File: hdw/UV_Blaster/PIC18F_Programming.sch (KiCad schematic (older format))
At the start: 10 parts

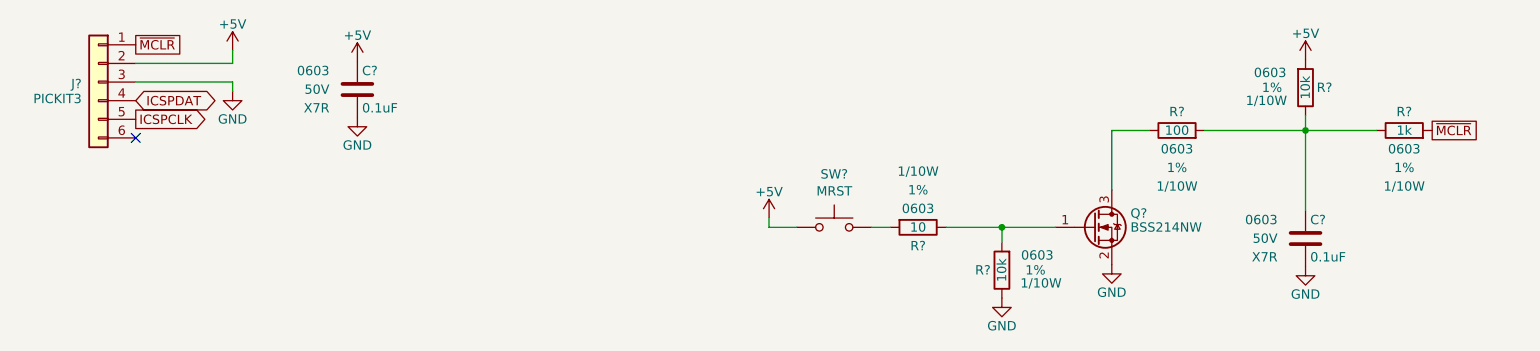
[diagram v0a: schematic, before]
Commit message: More sch work, netlist, part numbers, footprints
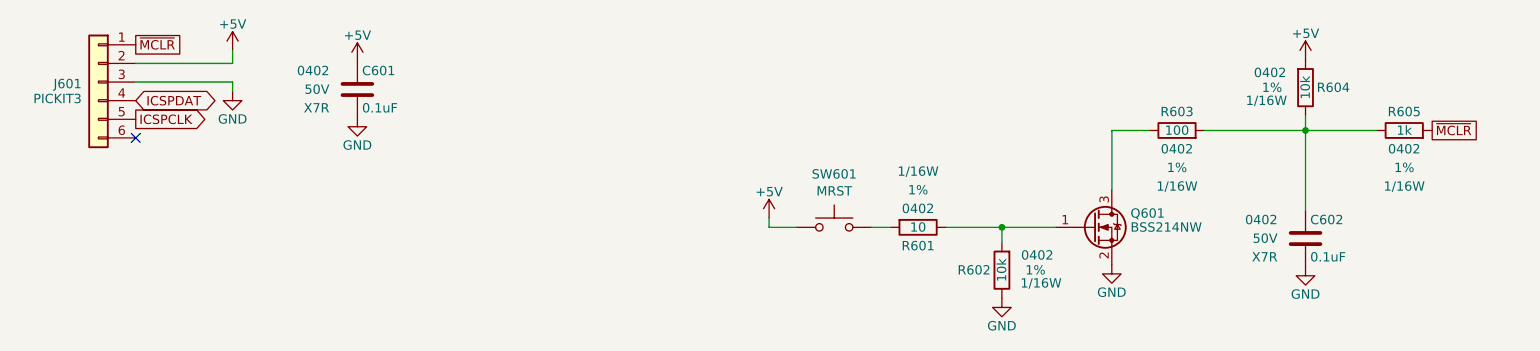
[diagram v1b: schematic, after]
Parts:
- C601, C602: renamed from C?; footprint Capacitors_SMD:C_0603 -> Capacitors_SMD:C_0402; Digi-Key PN 311-1344-1-ND -> 490-10701-1-ND; display_footprint 0603 -> 0402
- R601: renamed from R?; footprint Resistors_SMD:R_0603 -> Resistors_SMD:R_0402; Digi-Key PN YAG3351CT-ND -> 311-10.0LRCT-ND; Wattage 1/10W -> 1/16W; display_footprint 0603 -> 0402
- R602, R604: renamed from R?; footprint Resistors_SMD:R_0603 -> Resistors_SMD:R_0402; Digi-Key PN RMCF0603FT10K0CT-ND -> 541-3959-1-ND; Wattage 1/10W -> 1/16W; display_footprint 0603 -> 0402
- R603: renamed from R?; footprint Resistors_SMD:R_0603 -> Resistors_SMD:R_0402; Digi-Key PN A106047CT-ND -> 311-100LRCT-ND; Wattage 1/10W -> 1/16W; display_footprint 0603 -> 0402
- R605: renamed from R?; footprint Resistors_SMD:R_0603 -> Resistors_SMD:R_0402; Digi-Key PN RMCF0603FT1K00CT-ND -> P1.00KLCT-ND; Wattage 1/10W -> 1/16W; display_footprint 0603 -> 0402
- gave numbers to parts that had none: 3
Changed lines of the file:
@@
 encoding utf-8
 Sheet 6 14
-Title "QI Charger"
-Date "2019-01-03"
+Title "UV Blaster"
+Date "2020-05-07"
 Rev "A"
-Comp ""
+Comp "Drew Maatman"
 Comment1 ""
 Comment2 ""
@@
 $EndDescr
 $Comp
-L Connector_Generic:Conn_01x06 J?
+L Connector_Generic:Conn_01x06 J601
 U 1 1 5BB4A695
 P 1070 1990
-F 0 "J?" H 1160 1980 50  0000 L CNN
+F 0 "J601" H 1160 1980 50  0000 L CNN
 F 1 "PICKIT3" H 1160 1900 50  0000 L CNN
 F 2 "Custom Footprints Library:PICKIT3_Header" H 1070 1990 50  0001 C CNN
@@
 ICSPCLK
 $Comp
-L power:GND #PWR?
+L power:GND #PWR0602
 U 1 1 5BB4A7C4
 P 1790 2040
-F 0 "#PWR?" H 1790 1790 50  0001 C CNN
+F 0 "#PWR0602" H 1790 1790 50  0001 C CNN
 F 1 "GND" H 1790 1890 50  0000 C CNN
 F 2 "" H 1790 2040 50  0001 C CNN
@@
 NoConn ~ 1270 2290
 $Comp
-L Custom_Library:C_Custom C?
+L Custom_Library:C_Custom C601
 U 1 1 5BC13497
 P 2460 2030
-F 0 "C?" H 2485 2130 50  0000 L CNN
+F 0 "C601" H 2485 2130 50  0000 L CNN
 F 1 "0.1uF" H 2485 1930 50  0000 L CNN
-F 2 "Capacitors_SMD:C_0603" H 2498 1880 50  0001 C CNN
+F 2 "Capacitors_SMD:C_0402" H 2498 1880 50  0001 C CNN
 F 3 "" H 2485 2130 50  0001 C CNN
-F 4 "0603" H 2310 2130 50  0000 R CNN "display_footprint"
+F 4 "0402" H 2310 2130 50  0000 R CNN "display_footprint"
 F 5 "50V" H 2310 2030 50  0000 R CNN "Voltage"
 F 6 "X7R" H 2310 1930 50  0000 R CNN "Dielectric"
-F 7 "311-1344-1-ND" H 2885 2530 60  0001 C CNN "Digi-Key PN"
+F 7 "490-10701-1-ND" H 2885 2530 60  0001 C CNN "Digi-Key PN"
 	1    2460 2030
 	1    0    0    -1
 $EndComp
 $Comp
-L power:GND #PWR?
+L power:GND #PWR0604
 U 1 1 5BC1349E
 P 2460 2180
-F 0 "#PWR?" H 2460 1930 50  0001 C CNN
+F 0 "#PWR0604" H 2460 1930 50  0001 C CNN
 F 1 "GND" H 2460 2030 50  0000 C CNN
 F 2 "" H 2460 2180 50  0001 C CNN
@@
 AR Path="/5BAAE16C/5BC152E5" Ref="R?"  Part="1"
 AR Path="/5C1D5CB6/5BC152E5" Ref="R?"  Part="1"
-AR Path="/5E9E1D6A/5BC152E5" Ref="R?"  Part="1"
-F 0 "R?" H 7490 2020 50  0000 R CNN
+AR Path="/5E9E1D6A/5BC152E5" Ref="R604"  Part="1"
+F 0 "R604" H 7490 2020 50  0000 R CNN
 F 1 "10k" V 7550 2020 50  0000 C CNN
-F 2 "Resistors_SMD:R_0603" H 7550 2020 50  0001 C CNN
+F 2 "Resistors_SMD:R_0402" H 7550 2020 50  0001 C CNN
 F 3 "" H 7550 2020 50  0001 C CNN
-F 4 "0603" H 7740 2100 50  0000 C CNN "display_footprint"
+F 4 "0402" H 7740 2100 50  0000 C CNN "display_footprint"
 F 5 "1%" H 7730 2020 50  0000 C CNN "Tolerance"
-F 6 "1/10W" H 7760 1950 50  0000 C CNN "Wattage"
-F 7 "RMCF0603FT10K0CT-ND" H 7850 2420 60  0001 C CNN "Digi-Key PN"
+F 6 "1/16W" H 7760 1950 50  0000 C CNN "Wattage"
+F 7 "541-3959-1-ND" H 7850 2420 60  0001 C CNN "Digi-Key PN"
 	1    7550 2020
 	-1   0    0    -1
 $EndComp
 $Comp
-L Custom_Library:C_Custom C?
+L Custom_Library:C_Custom C602
 U 1 1 5BC1574E
 P 7550 2830
-F 0 "C?" H 7575 2930 50  0000 L CNN
+F 0 "C602" H 7575 2930 50  0000 L CNN
 F 1 "0.1uF" H 7575 2730 50  0000 L CNN
-F 2 "Capacitors_SMD:C_0603" H 7588 2680 50  0001 C CNN
+F 2 "Capacitors_SMD:C_0402" H 7588 2680 50  0001 C CNN
 F 3 "" H 7575 2930 50  0001 C CNN
-F 4 "0603" H 7400 2930 50  0000 R CNN "display_footprint"
+F 4 "0402" H 7400 2930 50  0000 R CNN "display_footprint"
 F 5 "50V" H 7400 2830 50  0000 R CNN "Voltage"
 F 6 "X7R" H 7400 2730 50  0000 R CNN "Dielectric"
-F 7 "311-1344-1-ND" H 7975 3330 60  0001 C CNN "Digi-Key PN"
+F 7 "490-10701-1-ND" H 7975 3330 60  0001 C CNN "Digi-Key PN"
 	1    7550 2830
 	1    0    0    -1
 $EndComp
 $Comp
-L power:GND #PWR?
+L power:GND #PWR0609
 U 1 1 5BC15E18
 P 7550 2980
-F 0 "#PWR?" H 7550 2730 50  0001 C CNN
+F 0 "#PWR0609" H 7550 2730 50  0001 C CNN
 F 1 "GND" H 7550 2830 50  0000 C CNN
 F 2 "" H 7550 2980 50  0001 C CNN
@@
 $EndComp
 $Comp
-L Custom_Library:R_Custom R?
+L Custom_Library:R_Custom R605
 U 1 1 5BC16316
 P 8080 2250
-F 0 "R?" V 7980 2250 50  0000 C CNN
+F 0 "R605" V 7980 2250 50  0000 C CNN
 F 1 "1k" V 8080 2250 50  0000 C CNN
-F 2 "Resistors_SMD:R_0603" H 8080 2250 50  0001 C CNN
+F 2 "Resistors_SMD:R_0402" H 8080 2250 50  0001 C CNN
 F 3 "" H 8080 2250 50  0001 C CNN
-F 4 "0603" V 8180 2250 50  0000 C CNN "display_footprint"
+F 4 "0402" V 8180 2250 50  0000 C CNN "display_footprint"
 F 5 "1%" V 8280 2250 50  0000 C CNN "Tolerance"
-F 6 "1/10W" V 8380 2250 50  0000 C CNN "Wattage"
-F 7 "RMCF0603FT1K00CT-ND" H 8380 2650 60  0001 C CNN "Digi-Key PN"
+F 6 "1/16W" V 8380 2250 50  0000 C CNN "Wattage"
+F 7 "P1.00KLCT-ND" H 8380 2650 60  0001 C CNN "Digi-Key PN"
 	1    8080 2250
 	0    1    1    0
@@
 ~MCLR
 $Comp
-L Switch:SW_Push SW?
+L Switch:SW_Push SW601
 U 1 1 5BC17B44
 P 5020 2770
-F 0 "SW?" H 5020 3055 50  0000 C CNN
+F 0 "SW601" H 5020 3055 50  0000 C CNN
 F 1 "MRST" H 5020 2964 50  0000 C CNN
 F 2 "Buttons_Switches_THT:SW_PUSH_6mm" H 5020 2970 50  0001 C CNN
@@
 $EndComp
 $Comp
-L Custom_Library:R_Custom R?
+L Custom_Library:R_Custom R603
 U 1 1 5BC190FF
 P 6860 2250
-F 0 "R?" V 6760 2250 50  0000 C CNN
+F 0 "R603" V 6760 2250 50  0000 C CNN
 F 1 "100" V 6860 2250 50  0000 C CNN
-F 2 "Resistors_SMD:R_0603" H 6860 2250 50  0001 C CNN
+F 2 "Resistors_SMD:R_0402" H 6860 2250 50  0001 C CNN
 F 3 "" H 6860 2250 50  0001 C CNN
-F 4 "0603" V 6960 2250 50  0000 C CNN "display_footprint"
+F 4 "0402" V 6960 2250 50  0000 C CNN "display_footprint"
 F 5 "1%" V 7060 2250 50  0000 C CNN "Tolerance"
-F 6 "1/10W" V 7160 2250 50  0000 C CNN "Wattage"
-F 7 "A106047CT-ND" H 7160 2650 60  0001 C CNN "Digi-Key PN"
+F 6 "1/16W" V 7160 2250 50  0000 C CNN "Wattage"
+F 7 "311-100LRCT-ND" H 7160 2650 60  0001 C CNN "Digi-Key PN"
 	1    6860 2250
 	0    1    1    0
@@
 AR Path="/5BB844FD/5BE087BA" Ref="Q?"  Part="1"
 AR Path="/5C1D5CB6/5BE087BA" Ref="Q?"  Part="1"
-AR Path="/5E9E1D6A/5BE087BA" Ref="Q?"  Part="1"
-F 0 "Q?" H 6610 2845 50  0000 L CNN
+AR Path="/5E9E1D6A/5BE087BA" Ref="Q601"  Part="1"
+F 0 "Q601" H 6610 2845 50  0000 L CNN
 F 1 "BSS214NW" H 6610 2770 50  0000 L CNN
 F 2 "TO_SOT_Packages_SMD:SOT-323_SC-70" H 6610 2695 50  0001 L CIN
@@
 $EndComp
 $Comp
-L power:GND #PWR?
+L power:GND #PWR0607
 U 1 1 5BE087C1
 P 6510 2970
-F 0 "#PWR?" H 6510 2720 50  0001 C CNN
+F 0 "#PWR0607" H 6510 2720 50  0001 C CNN
 F 1 "GND" H 6510 2820 50  0000 C CNN
 F 2 "" H 6510 2970 50  0001 C CNN
@@
 $EndComp
 $Comp
-L Custom_Library:R_Custom R?
+L Custom_Library:R_Custom R601
 U 1 1 5BE087CB
 P 5470 2770
-F 0 "R?" V 5370 2770 50  0000 C CNN
+F 0 "R601" V 5370 2770 50  0000 C CNN
 F 1 "10" V 5470 2770 50  0000 C CNN
-F 2 "Resistors_SMD:R_0603" H 5470 2770 50  0001 C CNN
+F 2 "Resistors_SMD:R_0402" H 5470 2770 50  0001 C CNN
 F 3 "" H 5470 2770 50  0001 C CNN
-F 4 "0603" V 5570 2770 50  0000 C CNN "display_footprint"
+F 4 "0402" V 5570 2770 50  0000 C CNN "display_footprint"
 F 5 "1%" V 5670 2770 50  0000 C CNN "Tolerance"
-F 6 "1/10W" V 5770 2770 50  0000 C CNN "Wattage"
-F 7 "YAG3351CT-ND" H 5770 3170 60  0001 C CNN "Digi-Key PN"
+F 6 "1/16W" V 5770 2770 50  0000 C CNN "Wattage"
+F 7 "311-10.0LRCT-ND" H 5770 3170 60  0001 C CNN "Digi-Key PN"
 	1    5470 2770
 	0    -1   -1   0
@@
 AR Path="/5BB844FD/5BE087D6" Ref="R?"  Part="1"
 AR Path="/5C1D5CB6/5BE087D6" Ref="R?"  Part="1"
-AR Path="/5E9E1D6A/5BE087D6" Ref="R?"  Part="1"
-F 0 "R?" H 5860 3000 50  0000 R CNN
+AR Path="/5E9E1D6A/5BE087D6" Ref="R602"  Part="1"
+F 0 "R602" H 5860 3000 50  0000 R CNN
 F 1 "10k" V 5920 3000 50  0000 C CNN
-F 2 "Resistors_SMD:R_0603" H 5920 3000 50  0001 C CNN
+F 2 "Resistors_SMD:R_0402" H 5920 3000 50  0001 C CNN
 F 3 "" H 5920 3000 50  0001 C CNN
-F 4 "0603" H 6110 3080 50  0000 C CNN "display_footprint"
+F 4 "0402" H 6110 3080 50  0000 C CNN "display_footprint"
 F 5 "1%" H 6100 3000 50  0000 C CNN "Tolerance"
-F 6 "1/10W" H 6130 2930 50  0000 C CNN "Wattage"
-F 7 "RMCF0603FT10K0CT-ND" H 6220 3400 60  0001 C CNN "Digi-Key PN"
+F 6 "1/16W" H 6130 2930 50  0000 C CNN "Wattage"
+F 7 "541-3959-1-ND" H 6220 3400 60  0001 C CNN "Digi-Key PN"
 	1    5920 3000
 	1    0    0    -1
 $EndComp
 $Comp
-L power:GND #PWR?
+L power:GND #PWR0606
 U 1 1 5BE087DD
 P 5920 3150
-F 0 "#PWR?" H 5920 2900 50  0001 C CNN
+F 0 "#PWR0606" H 5920 2900 50  0001 C CNN
 F 1 "GND" H 5920 3000 50  0000 C CNN
 F 2 "" H 5920 3150 50  0001 C CNN
@@
 	4670 2770 4820 2770
 $Comp
-L power:+5V #PWR?
+L power:+5V #PWR0608
 U 1 1 5C1E843D
 P 7550 1870
-F 0 "#PWR?" H 7550 1720 50  0001 C CNN
+F 0 "#PWR0608" H 7550 1720 50  0001 C CNN
 F 1 "+5V" H 7550 2010 50  0000 C CNN
 F 2 "" H 7550 1870 50  0001 C CNN
@@
 $EndComp
 $Comp
-L power:+5V #PWR?
+L power:+5V #PWR0605
 U 1 1 5C1E8465
 P 4670 2720
-F 0 "#PWR?" H 4670 2570 50  0001 C CNN
+F 0 "#PWR0605" H 4670 2570 50  0001 C CNN
 F 1 "+5V" H 4670 2860 50  0000 C CNN
 F 2 "" H 4670 2720 50  0001 C CNN
@@
 $EndComp
 $Comp
-L power:+5V #PWR?
+L power:+5V #PWR0603
 U 1 1 5C1E849C
 P 2460 1880
-F 0 "#PWR?" H 2460 1730 50  0001 C CNN
+F 0 "#PWR0603" H 2460 1730 50  0001 C CNN
 F 1 "+5V" H 2460 2020 50  0000 C CNN
 F 2 "" H 2460 1880 50  0001 C CNN
@@
 $EndComp
 $Comp
-L power:+5V #PWR?
+L power:+5V #PWR0601
 U 1 1 5C1E850A
 P 1790 1820
-F 0 "#PWR?" H 1790 1670 50  0001 C CNN
+F 0 "#PWR0601" H 1790 1670 50  0001 C CNN
 F 1 "+5V" H 1790 1960 50  0000 C CNN
 F 2 "" H 1790 1820 50  0001 C CNN
